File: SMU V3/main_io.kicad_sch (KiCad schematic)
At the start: 6 parts, among them J1 Connector, J2 Connector

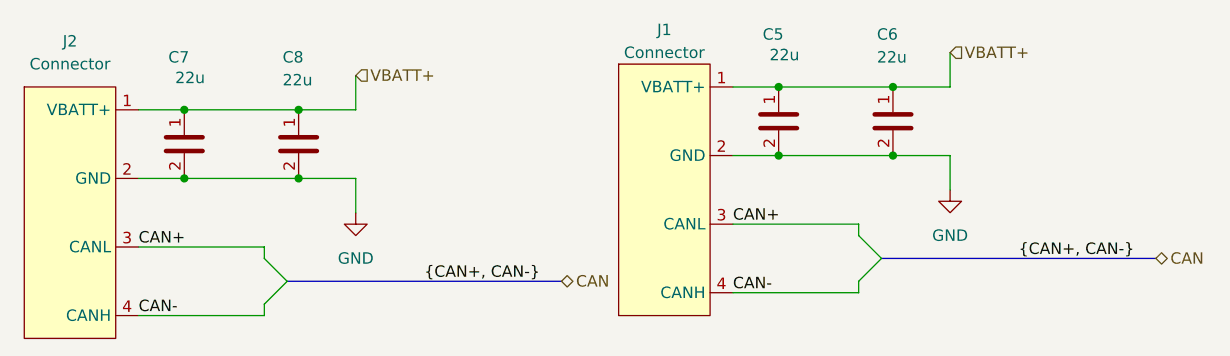
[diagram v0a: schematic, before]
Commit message: improved V3
added uart/spi test points and status leds
removed main 3v3 ldo
added silkscreen
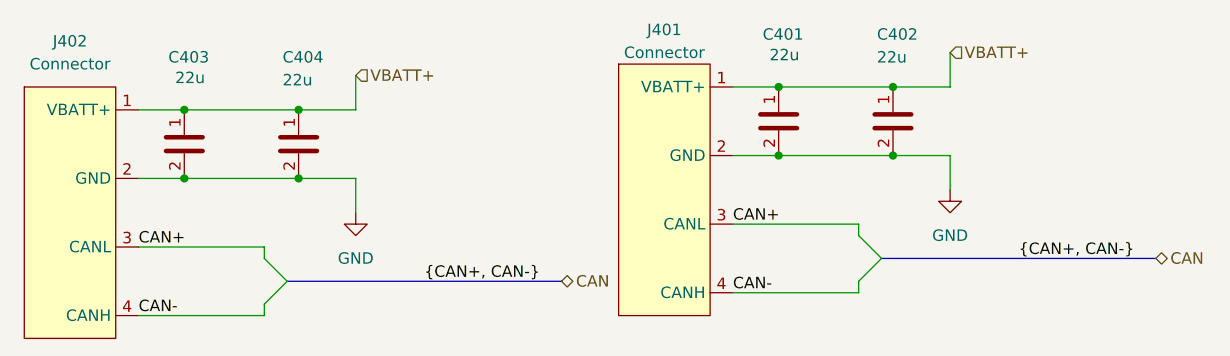
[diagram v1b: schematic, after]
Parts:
- renumbered C5 to C401, C6 to C402, C7 to C403, C8 to C404, J1 to J401, J2 to J402
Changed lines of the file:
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@@
 		(in_pos_files yes)
 		(dnp no)
-		(property "Reference" "C5"
+		(property "Reference" "C401"
 			(at 156.972 84.3279 0)
 			(show_name no)
@@
 			(project "SMU V3"
 				(path "/1f58b889-96e6-4877-90a3-5a655db5910b/aa7c806b-d8c1-4e28-abf2-720fa257e015"
-					(reference "C5")
+					(reference "C401")
 					(unit 1)
 				)
@@
 		(in_pos_files yes)
 		(dnp no)
-		(property "Reference" "C7"
+		(property "Reference" "C403"
 			(at 90.932 86.8679 0)
 			(show_name no)
@@
 			(project "SMU V3"
 				(path "/1f58b889-96e6-4877-90a3-5a655db5910b/aa7c806b-d8c1-4e28-abf2-720fa257e015"
-					(reference "C7")
+					(reference "C403")
 					(unit 1)
 				)
@@
 		(in_pos_files yes)
 		(dnp no)
-		(property "Reference" "C8"
+		(property "Reference" "C404"
 			(at 103.632 86.868 0)
 			(show_name no)
@@
 			(project "SMU V3"
 				(path "/1f58b889-96e6-4877-90a3-5a655db5910b/aa7c806b-d8c1-4e28-abf2-720fa257e015"
-					(reference "C8")
+					(reference "C404")
 					(unit 1)
 				)
@@
 		(dnp no)
 		(fields_autoplaced yes)
-		(property "Reference" "#PWR07"
+		(property "Reference" "#PWR0402"
 			(at 111.76 110.49 0)
 			(hide yes)
@@
 			(project "SMU V3"
 				(path "/1f58b889-96e6-4877-90a3-5a655db5910b/aa7c806b-d8c1-4e28-abf2-720fa257e015"
-					(reference "#PWR07")
+					(reference "#PWR0402")
 					(unit 1)
 				)
@@
 		(dnp no)
 		(fields_autoplaced yes)
-		(property "Reference" "#PWR08"
+		(property "Reference" "#PWR0401"
 			(at 177.8 107.95 0)
 			(hide yes)
@@
 			(project "SMU V3"
 				(path "/1f58b889-96e6-4877-90a3-5a655db5910b/aa7c806b-d8c1-4e28-abf2-720fa257e015"
-					(reference "#PWR08")
+					(reference "#PWR0401")
 					(unit 1)
 				)
@@
 		(dnp no)
 		(fields_autoplaced yes)
-		(property "Reference" "J2"
+		(property "Reference" "J402"
 			(at 80.01 85.09 0)
 			(show_name no)
@@
 			(project "SMU V3"
 				(path "/1f58b889-96e6-4877-90a3-5a655db5910b/aa7c806b-d8c1-4e28-abf2-720fa257e015"
-					(reference "J2")
+					(reference "J402")
 					(unit 1)
 				)
@@
 		(in_pos_files yes)
 		(dnp no)
-		(property "Reference" "C6"
+		(property "Reference" "C402"
 			(at 169.672 84.328 0)
 			(show_name no)
@@
 			(project "SMU V3"
 				(path "/1f58b889-96e6-4877-90a3-5a655db5910b/aa7c806b-d8c1-4e28-abf2-720fa257e015"
-					(reference "C6")
+					(reference "C402")
 					(unit 1)
 				)
@@
 		(dnp no)
 		(fields_autoplaced yes)
-		(property "Reference" "J1"
+		(property "Reference" "J401"
 			(at 146.05 83.82 0)
 			(show_name no)
@@
 			(project "SMU V3"
 				(path "/1f58b889-96e6-4877-90a3-5a655db5910b/aa7c806b-d8c1-4e28-abf2-720fa257e015"
-					(reference "J1")
+					(reference "J401")
 					(unit 1)
 				)
